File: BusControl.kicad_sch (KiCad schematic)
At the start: 51 parts, among them U17 74LVC74AD, U18 74LVC74AD, U19 74LVC74AD, U20 74LVC86AD, U21 74LVC32AD, U22 74LVC02AD, U23 74LVC00AD, U24 74LVC125AD, U25 74LVC32AD, U26 74LVC125AD, U34 74LVC32AD, U35 74LVC74AD, U36 74LVC74AD, U37 74LVC74AD, U42 74LVC32AD

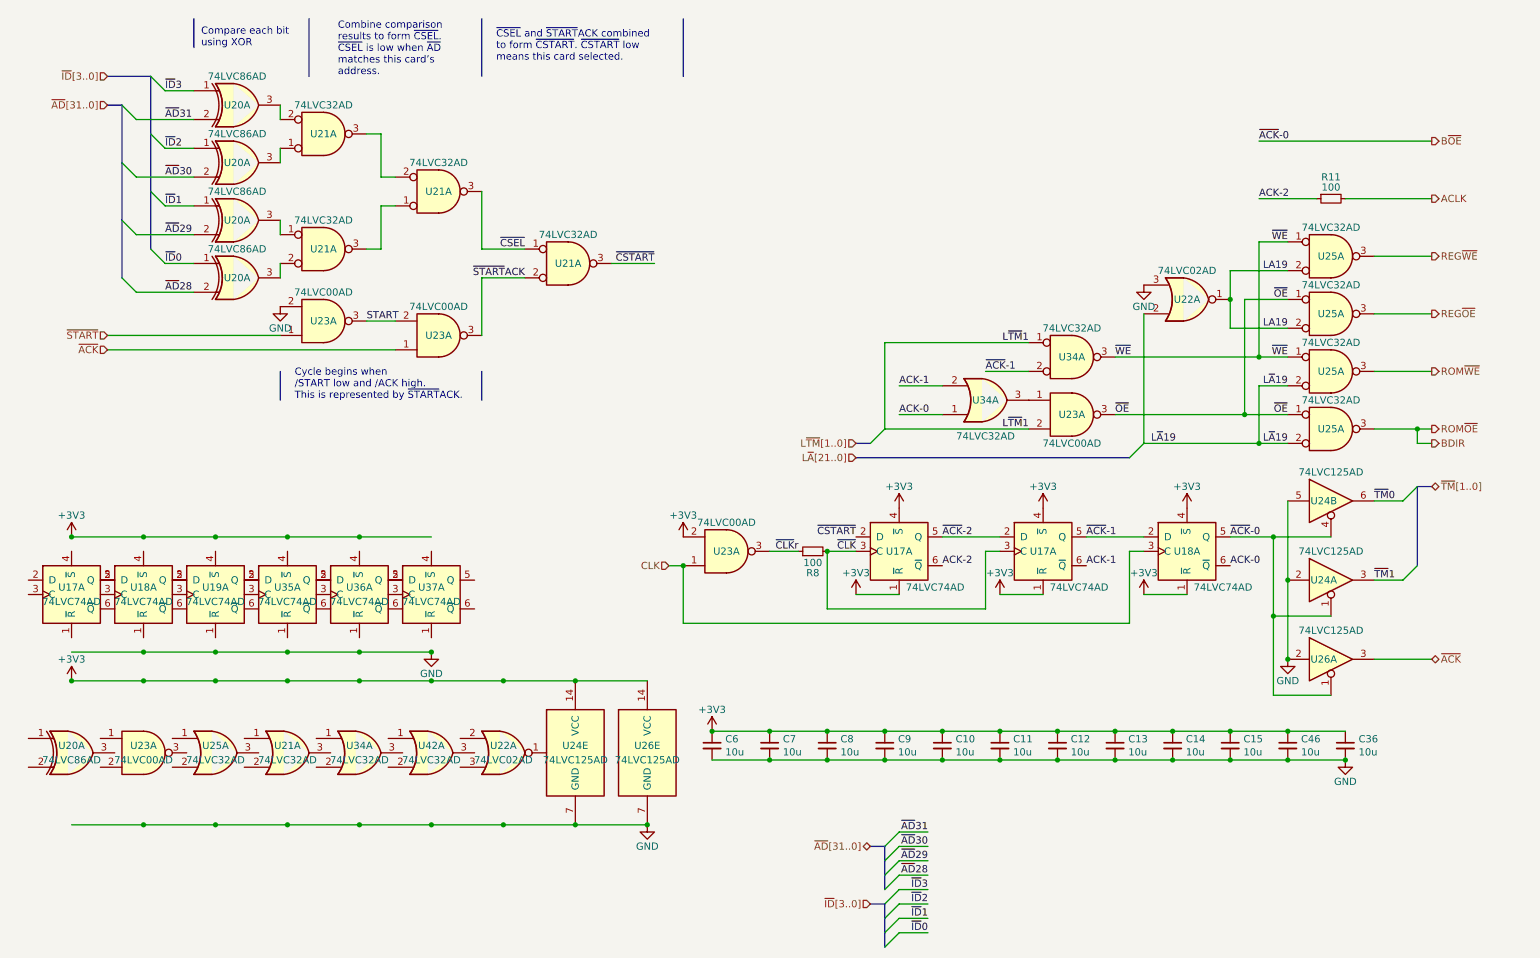
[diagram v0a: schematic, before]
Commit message: Prototype with 74xx
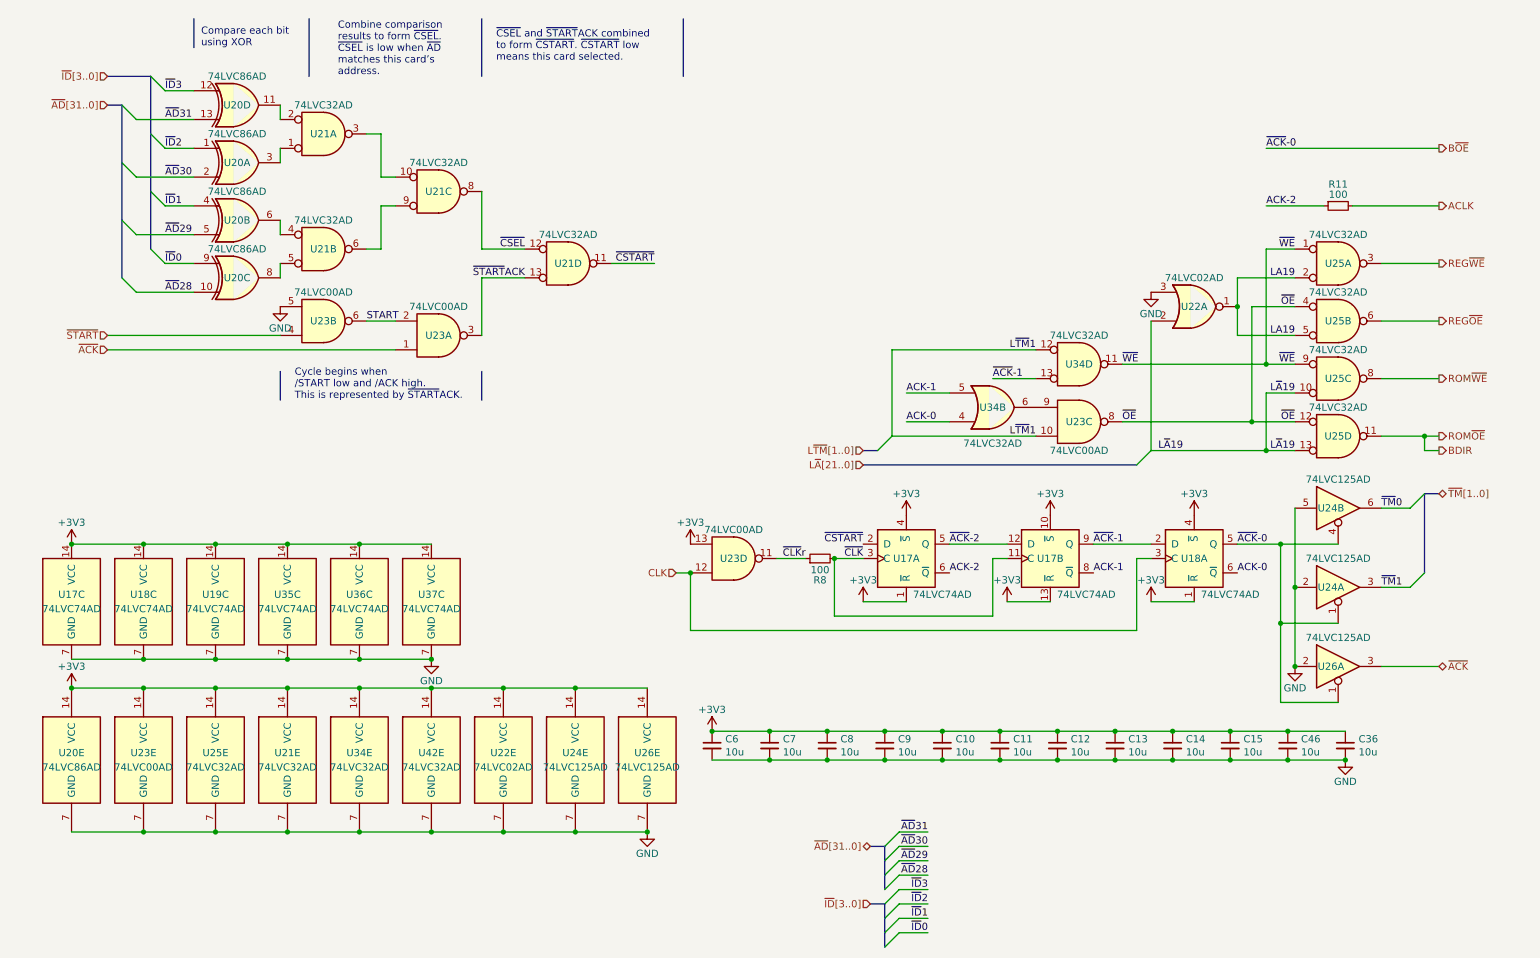
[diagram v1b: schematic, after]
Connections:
- net +3V3: now also U17.10 (~{S}), U17.13 (~{R}), U17.14 (VCC), U18.14 (VCC), U19.14 (VCC), U20.14 (VCC), U21.14 (VCC), U22.14 (VCC), U23.13, U23.14 (VCC), U25.14 (VCC), U34.14 (VCC), U35.14 (VCC), U36.14 (VCC), U37.14 (VCC), U42.14 (VCC); no longer U17.1 (~{R}), U17.4 (~{S}), U23.2
- net ACK-0: now also U34.4; no longer U34.1
- net ACK-1: now also U17.8 (~{Q}), U34.5; no longer U17.6 (~{Q}), U34.2
- net BDIR: now also U25.11; no longer U25.3
- net CLK: now also U23.12; no longer U23.1
- net GND: now also U17.7 (GND), U18.7 (GND), U19.7 (GND), U20.7 (GND), U21.7 (GND), U22.7 (GND), U23.5, U23.7 (GND), U25.7 (GND), U34.7 (GND), U35.7 (GND), U36.7 (GND), U37.7 (GND), U42.7 (GND); no longer U23.2
- net LA19: now also U25.5; no longer U25.2
- net L~{A}19: now also U25.10, U25.13; no longer U25.2, U25.2
- net L~{TM}1: now also U23.10, U34.12; no longer U23.2, U34.1
- net REG~{OE}: now also U25.6; no longer U25.3
- net ROM~{WE}: now also U25.8; no longer U25.3
- net START: now also U23.6; no longer U23.3
- net ~{ACK}-1: now also U17.9 (Q), U34.13; no longer U17.5 (Q), U34.2
- net ~{ACK}-2: now also U17.12 (D); no longer U17.2 (D)
- net ~{AD}28: now also U20.10; no longer U20.2
- net ~{AD}29: now also U20.5; no longer U20.2
- net ~{AD}31: now also U20.13; no longer U20.2
- net ~{CLK}: now also U17.11 (C); no longer U17.3 (C)
- net ~{CLK}r: now also U23.11; no longer U23.3
- net ~{CSEL}: now also U21.12, U21.8; no longer U21.1, U21.3
- net ~{CSTART}: now also U21.11; no longer U21.3
- net ~{ID}0: now also U20.9; no longer U20.1
- net ~{ID}1: now also U20.4; no longer U20.1
- net ~{ID}3: now also U20.12; no longer U20.1
- net ~{OE}: now also U23.8, U25.12, U25.4; no longer U23.3, U25.1, U25.1
- net ~{START}: now also U23.4; no longer U23.1
- net ~{START}ACK: now also U21.13; no longer U21.2
- net ~{WE}: now also U25.9, U34.11; no longer U25.1, U34.3
- net at U21.3: now also U21.10; no longer U21.2
- net at U21.2: now also U20.11; no longer U20.3
- new net: U23.9, U34.6
- new net: U21.6, U21.9
- new net: U20.6, U21.4
- new net: U20.8, U21.5
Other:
- moved on the sheet: R11, R8, U17A, U17B, U18A, U22A, U23C, U23D, U24A, U24B, U24E, U25A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

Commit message: idk
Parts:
- added U? (x2): GAL16V8, symbol GW_PLD:GAL16V8
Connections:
- net ACK-1: now also U?.18 (I/O)
- net ACK-2: now also U?.19 (I/O)
- net BDIR: now also U?.14 (I/O)
- net B~{OE}: now also U?.19 (I/O), U?.6 (IN)
- net CLK: now also U?.1 (CLK/IN), U?.2 (IN)
- net GND: now also U?.10 (GND), U?.10 (GND), U?.11 (IN/~{OE}), U?.11 (IN/~{OE})
- net L~{A}19: now also U?.3 (IN)
- net L~{TM}1: now also U?.2 (IN)
- net REG~{OE}: now also U?.16 (I/O)
- net REG~{WE}: now also U?.17 (I/O)
- net ROM~{WE}: now also U?.15 (I/O)
- net ~{ACK}: now also U?.4 (IN)
- net ~{CLK}: now also U?.1 (CLK/IN), U?.14 (I/O)
- net ~{START}: now also U?.5 (IN)
- new net +5V: U?.20 (Vcc), U?.20 (Vcc)
- new net ACK~{OE}: U?.18 (I/O)
- new net NMRQ: U?.15 (I/O)
- new net RD~{IE}: U?.6 (IN)
- new net WR~{IE}: U?.5 (IN)
- new net ~{M}28: U?.9 (IN)
- new net ~{M}29: U?.12 (I/O)
- new net ~{M}30: U?.8 (IN)
- new net ~{M}31: U?.7 (IN)
- new net ~{RDREQ}: U?.4 (IN)
- new net ~{RDREQ}N: U?.16 (I/O)
- new net ~{WRREQ}: U?.3 (IN)
- new net ~{WRREQ}N: U?.17 (I/O)
